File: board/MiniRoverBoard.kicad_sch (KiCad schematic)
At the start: 0 parts

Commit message: small fixes + 3.3V line
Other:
- added sheet MCU (MCU.kicad_sch)
- added sheet Power (Mini-Rover.kicad_sch)
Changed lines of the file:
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@@
 	(generator_version "9.0")
 	(paper "A4")
+	(sheet
+		(at 115.57 67.31)
+		(size 44.45 40.64)
+		(exclude_from_sim no)
+		(in_bom yes)
+		(on_board yes)
+		(dnp no)
+		(fields_autoplaced yes)
+		(stroke
+			(width 0.1524)
+			(type solid)
+		)
+		(fill
+			(color 0 0 0 0.0000)
+		)
+		(property "Sheetname" "MCU"
+			(at 115.57 66.5984 0)
+			(effects
+				(font
+					(size 1.27 1.27)
+				)
+				(justify left bottom)
+			)
+		)
+		(property "Sheetfile" "MCU.kicad_sch"
+			(at 115.57 108.5346 0)
+			(effects
+				(font
+					(size 1.27 1.27)
+				)
+				(justify left top)
+			)
+		)
+		(instances
+			(project "MiniRoverBoard"
+				(path "/fbd9c71c-f200-4aab-a303-9f269bc9de13"
+					(page "3")
+				)
+			)
+		)
+	)
+	(sheet
+		(at 166.37 66.04)
+		(size 36.83 40.64)
+		(exclude_from_sim no)
+		(in_bom yes)
+		(on_board yes)
+		(dnp no)
+		(fields_autoplaced yes)
+		(stroke
+			(width 0.1524)
+			(type solid)
+		)
+		(fill
+			(color 0 0 0 0.0000)
+		)
+		(property "Sheetname" "Power"
+			(at 166.37 65.3284 0)
+			(effects
+				(font
+					(size 1.27 1.27)
+				)
+				(justify left bottom)
+			)
+		)
+		(property "Sheetfile" "Mini-Rover.kicad_sch"
+			(at 166.37 107.2646 0)
+			(effects
+				(font
+					(size 1.27 1.27)
+				)
+				(justify left top)
+			)
+		)
+		(instances
+			(project "MiniRoverBoard"
+				(path "/fbd9c71c-f200-4aab-a303-9f269bc9de13"
+					(page "2")
+				)
+			)
+		)
+	)
 	(sheet_instances
 		(path "/"

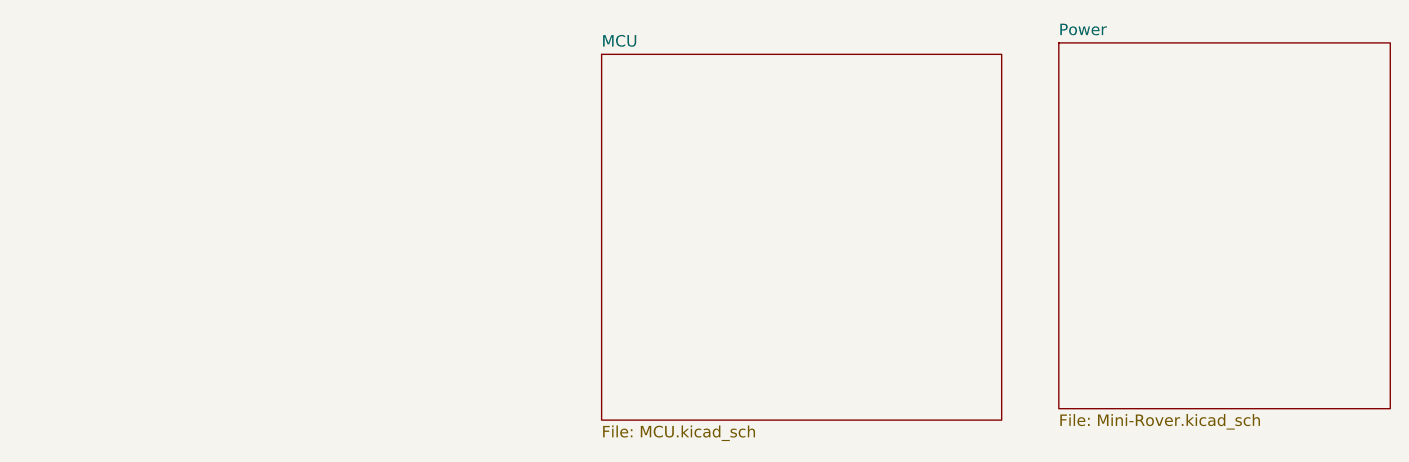
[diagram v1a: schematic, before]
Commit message: Add cell sensing opamp
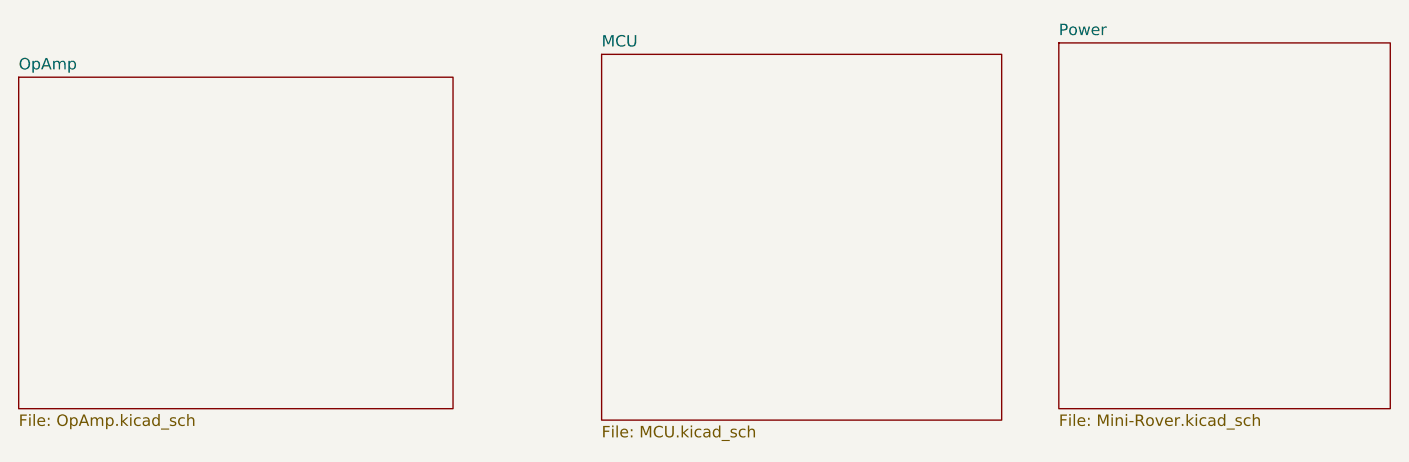
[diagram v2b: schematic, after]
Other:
- added sheet OpAmp (OpAmp.kicad_sch)
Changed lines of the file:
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@@
 	(paper "A4")
+	(sheet
+		(at 50.8 69.85)
+		(size 48.26 36.83)
+		(exclude_from_sim no)
+		(in_bom yes)
+		(on_board yes)
+		(dnp no)
+		(fields_autoplaced yes)
+		(stroke
+			(width 0.1524)
+			(type solid)
+		)
+		(fill
+			(color 0 0 0 0.0000)
+		)
+		(property "Sheetname" "OpAmp"
+			(at 50.8 69.1384 0)
+			(effects
+				(font
+					(size 1.27 1.27)
+				)
+				(justify left bottom)
+			)
+		)
+		(property "Sheetfile" "OpAmp.kicad_sch"
+			(at 50.8 107.2646 0)
+			(effects
+				(font
+					(size 1.27 1.27)
+				)
+				(justify left top)
+			)
+		)
+		(instances
+			(project "MiniRoverBoard"
+				(path "/fbd9c71c-f200-4aab-a303-9f269bc9de13"
+					(page "4")
+				)
+			)
+		)
+	)
 	(sheet
 		(at 115.57 67.31)
